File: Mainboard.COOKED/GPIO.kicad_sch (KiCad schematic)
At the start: 12 parts, among them J10 Conn_01x03_Pin, J11 Conn_01x03_Pin, J12 Conn_01x04_Pin, J13 Conn_01x04_Pin, J14 Conn_01x03_Pin, J7 Conn_01x04_Pin, J8 Conn_01x03_Pin, J9 Conn_01x04_Pin, U10 ULC0524P, U11 ULC0524P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

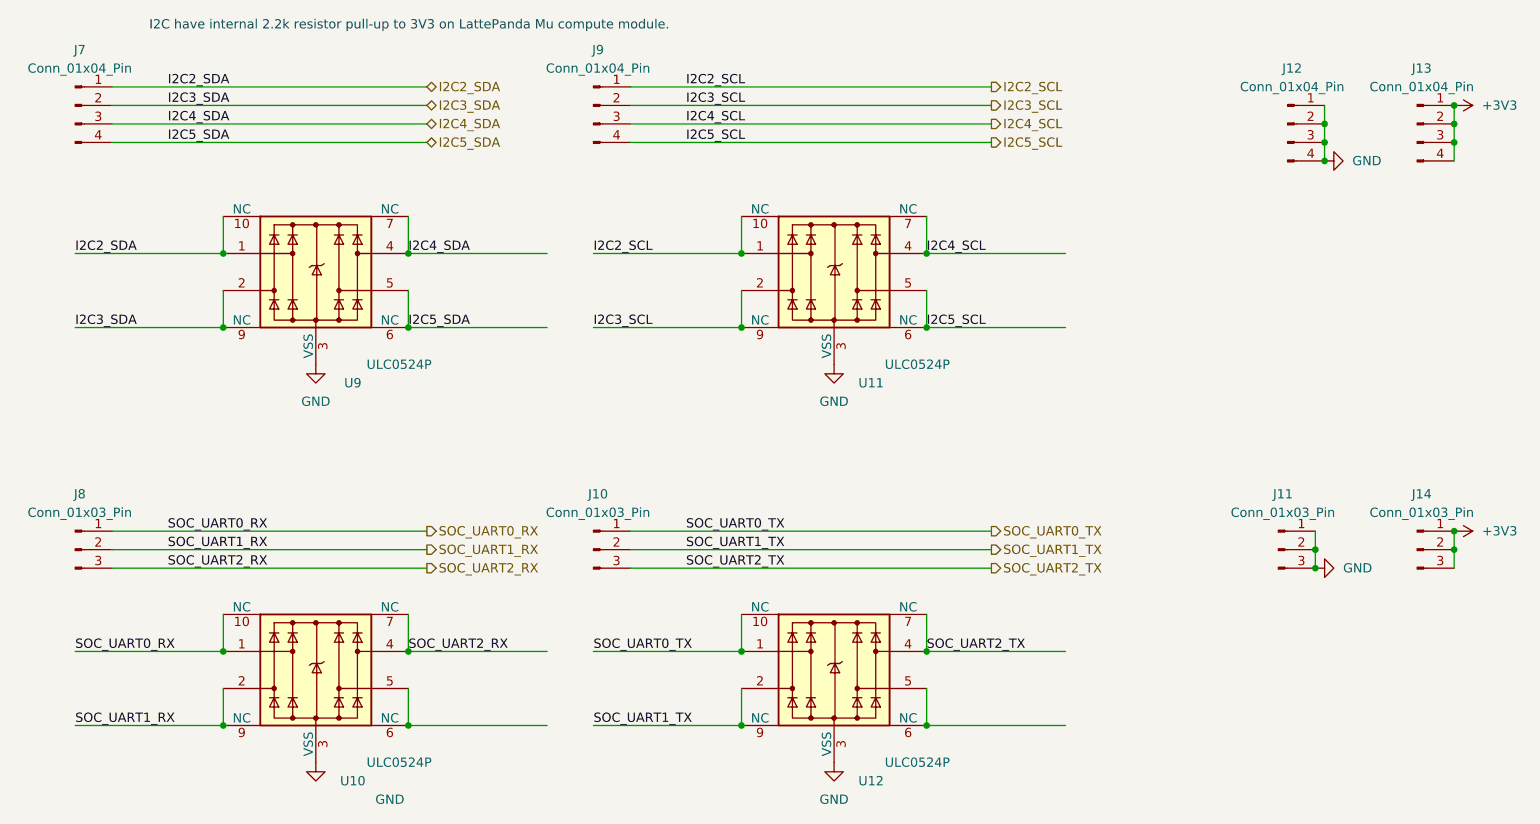
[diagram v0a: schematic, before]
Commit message: "Scrapped" the current Mainboard, seems to be very broken for no reason.
It is being kept for now so that work done for the displays can be copied over later.
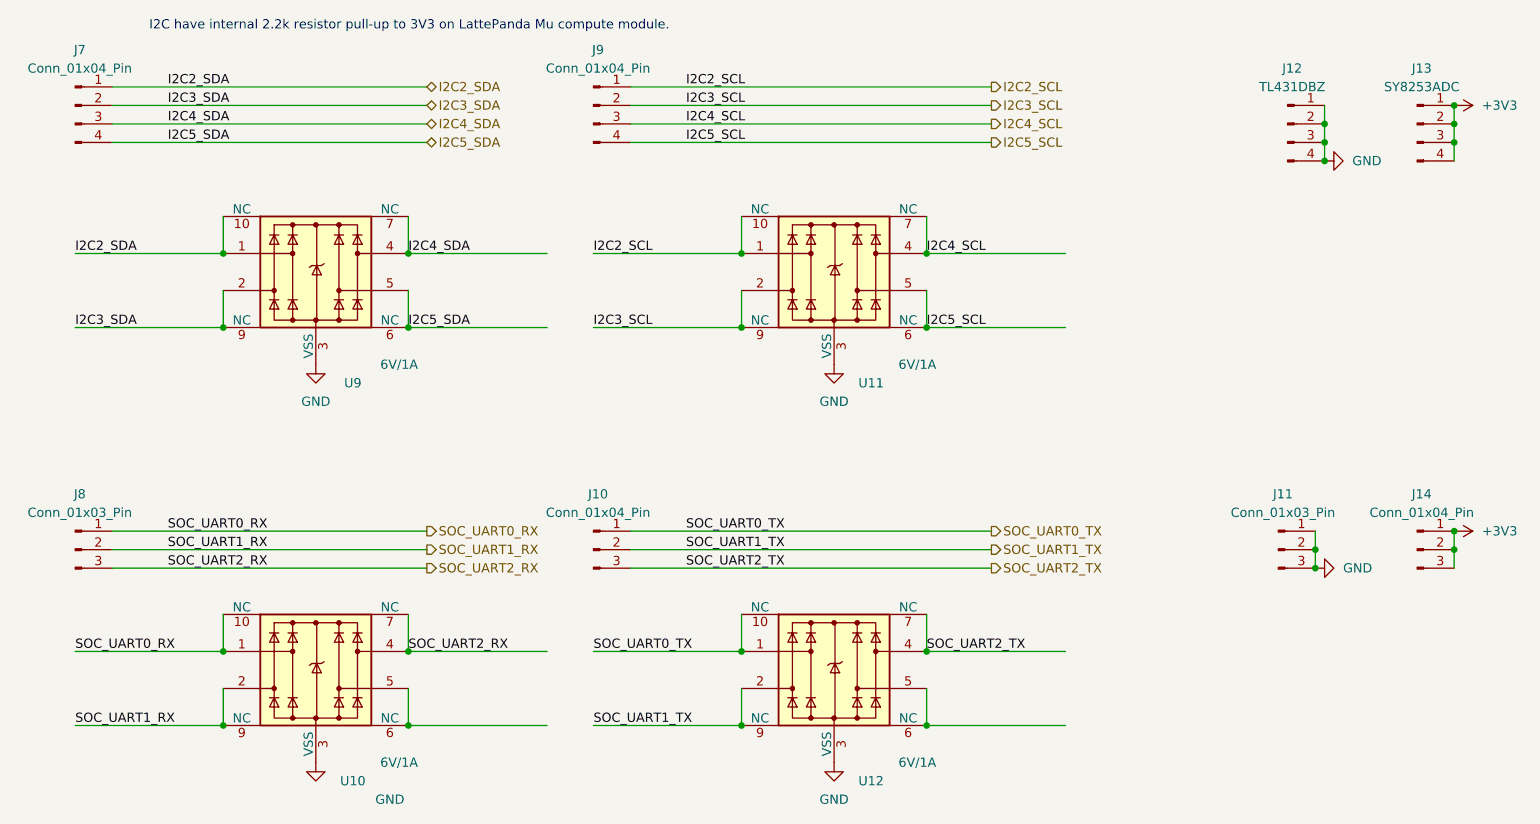
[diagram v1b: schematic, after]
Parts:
- J10: value Conn_01x03_Pin -> Conn_01x04_Pin; footprint A_HDJ_Library:PinHeader_1x03_P2.54mm_Vertical -> A_HDJ_Library:PinHeader_1x04_P2.54mm_Vertical; DF_Comment 2.54蓝色单排排针-3P -> 2.54绿色单排排针-4P
- J11: DF_Comment 2.54黑色单排排针-3P -> 2.54蓝色单排排针-3P
- J12: value Conn_01x04_Pin -> TL431DBZ; footprint A_HDJ_Library:PinHeader_1x04_P2.54mm_Vertical -> A_HDJ_Library:SOT-23; DF_Comment 2.54黑色单排排针-4P -> 参考电压-TL431ACDBZR-SOT23（丝印TAC）
- J13: value Conn_01x04_Pin -> SY8253ADC; footprint A_HDJ_Library:PinHeader_1x04_P2.54mm_Vertical -> A_HDJ_Library:TSOT-23-6; Buy_Link (none) -> https://item.szlcsc.com/94934.html; DF_Comment 2.54红色单排排针-4P -> DCDC同步降压芯片_SY8253ADC_TSOT23-6
- J14: value Conn_01x03_Pin -> Conn_01x04_Pin; footprint A_HDJ_Library:PinHeader_1x03_P2.54mm_Vertical -> A_HDJ_Library:PinHeader_1x04_P2.54mm_Vertical; DF_Comment 2.54红色单排排针-3P -> 2.54蓝色单排排针-4P
- J7: DF_Comment 2.54绿色单排排针-4P -> 2.54黑色单排排针-4P
- J8: DF_Comment 2.54绿色单排排针-3P -> 2.54红色单排排针-3P
- J9: DF_Comment 2.54蓝色单排排针-4P -> 2.54红色单排排针-4P
- U10, U11, U12, U9: value ULC0524P -> 6V/1A; footprint A_HDJ_Library:Diodes_UDFN-10_1.0x2.5mm_P0.5mm -> A_HDJ_Library:Fuse_0805_2012Metric; Buy_Link (none) -> https://item.szlcsc.com/947770.html; DF_Comment ESD静电保护IC-BV-ULC0524P-DFN2510-10L -> 0805贴片自恢复保险丝1A-6V_BSMD0805-100-6V; SCH_Show_Footprint (none) -> R0603
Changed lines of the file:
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@@
 			)
 		)
-		(property "Value" "Conn_01x03_Pin"
+		(property "Value" "Conn_01x04_Pin"
 			(at 290.195 223.52 0)
 			(show_name no)
@@
 			)
 		)
-		(property "Footprint" "A_HDJ_Library:PinHeader_1x03_P2.54mm_Vertical"
+		(property "Footprint" "A_HDJ_Library:PinHeader_1x04_P2.54mm_Vertical"
 			(at 289.56 228.6 0)
 			(hide yes)
@@
 			)
 		)
-		(property "DF_Comment" "2.54蓝色单排排针-3P"
+		(property "DF_Comment" "2.54绿色单排排针-4P"
 			(at 289.56 228.6 0)
 			(hide yes)
@@
 			)
 		)
-		(property "DF_Comment" "2.54蓝色单排排针-4P"
+		(property "DF_Comment" "2.54红色单排排针-4P"
 			(at 289.56 167.64 0)
 			(hide yes)
@@
 			)
 		)
-		(property "Value" "ULC0524P"
+		(property "Value" "6V/1A"
 			(at 262.89 203.2 0)
 			(show_name no)
@@
 			)
 		)
-		(property "Footprint" "A_HDJ_Library:Diodes_UDFN-10_1.0x2.5mm_P0.5mm"
+		(property "Footprint" "A_HDJ_Library:Fuse_0805_2012Metric"
 			(at 227.33 200.66 0)
 			(hide yes)
@@
 			)
 		)
-		(property "Datasheet" "https://www.diodes.com/assets/Datasheets/D3V3XA4B10LP.pdf"
+		(property "Datasheet" ""
 			(at 251.46 190.5 0)
 			(hide yes)
@@
 			)
 		)
-		(property "Buy_Link" ""
+		(property "Buy_Link" "https://item.szlcsc.com/947770.html"
 			(at 251.46 190.5 0)
 			(hide yes)
@@
 			)
 		)
-		(property "DF_Comment" "ESD静电保护IC-BV-ULC0524P-DFN2510-10L"
+		(property "DF_Comment" "0805贴片自恢复保险丝1A-6V_BSMD0805-100-6V"
 			(at 251.46 190.5 0)
 			(hide yes)
@@
 			)
 		)
-		(property "SCH_Show_Footprint" ""
+		(property "SCH_Show_Footprint" "R0603"
 			(at 251.46 190.5 0)
 			(hide yes)
@@
 			)
 		)
-		(property "Value" "ULC0524P"
+		(property "Value" "6V/1A"
 			(at 334.01 203.2 0)
 			(show_name no)
@@
 			)
 		)
-		(property "Footprint" "A_HDJ_Library:Diodes_UDFN-10_1.0x2.5mm_P0.5mm"
+		(property "Footprint" "A_HDJ_Library:Fuse_0805_2012Metric"
 			(at 298.45 200.66 0)
 			(hide yes)
@@
 			)
 		)
-		(property "Datasheet" "https://www.diodes.com/assets/Datasheets/D3V3XA4B10LP.pdf"
+		(property "Datasheet" ""
 			(at 322.58 190.5 0)
 			(hide yes)
@@
 			)
 		)
-		(property "Buy_Link" ""
+		(property "Buy_Link" "https://item.szlcsc.com/947770.html"
 			(at 322.58 190.5 0)
 			(hide yes)
@@
 			)
 		)
-		(property "DF_Comment" "ESD静电保护IC-BV-ULC0524P-DFN2510-10L"
+		(property "DF_Comment" "0805贴片自恢复保险丝1A-6V_BSMD0805-100-6V"
 			(at 322.58 190.5 0)
 			(hide yes)
@@
 			)
 		)
-		(property "SCH_Show_Footprint" ""
+		(property "SCH_Show_Footprint" "R0603"
 			(at 322.58 190.5 0)
 			(hide yes)
@@
 			)
 		)
-		(property "DF_Comment" "2.54绿色单排排针-4P"
+		(property "DF_Comment" "2.54黑色单排排针-4P"
 			(at 218.44 167.64 0)
 			(hide yes)
@@
 			)
 		)
-		(property "DF_Comment" "2.54绿色单排排针-3P"
+		(property "DF_Comment" "2.54红色单排排针-3P"
 			(at 218.44 228.6 0)
 			(hide yes)
@@
 			)
 		)
-		(property "DF_Comment" "2.54黑色单排排针-3P"
+		(property "DF_Comment" "2.54蓝色单排排针-3P"
 			(at 383.54 228.6 0)
 			(hide yes)
@@
 			)
 		)
-		(property "Value" "ULC0524P"
+		(property "Value" "6V/1A"
 			(at 262.89 257.81 0)
 			(show_name no)
@@
 			)
 		)
-		(property "Footprint" "A_HDJ_Library:Diodes_UDFN-10_1.0x2.5mm_P0.5mm"
+		(property "Footprint" "A_HDJ_Library:Fuse_0805_2012Metric"
 			(at 227.33 255.27 0)
 			(hide yes)
@@
 			)
 		)
-		(property "Datasheet" "https://www.diodes.com/assets/Datasheets/D3V3XA4B10LP.pdf"
+		(property "Datasheet" ""
 			(at 251.46 245.11 0)
 			(hide yes)
@@
 			)
 		)
-		(property "Buy_Link" ""
+		(property "Buy_Link" "https://item.szlcsc.com/947770.html"
 			(at 251.46 245.11 0)
 			(hide yes)
@@
 			)
 		)
-		(property "DF_Comment" "ESD静电保护IC-BV-ULC0524P-DFN2510-10L"
+		(property "DF_Comment" "0805贴片自恢复保险丝1A-6V_BSMD0805-100-6V"
 			(at 251.46 245.11 0)
 			(hide yes)
@@
 			)
 		)
-		(property "SCH_Show_Footprint" ""
+		(property "SCH_Show_Footprint" "R0603"
 			(at 251.46 245.11 0)
 			(hide yes)
@@
 			)
 		)
-		(property "Value" "Conn_01x04_Pin"
+		(property "Value" "SY8253ADC"
 			(at 403.225 165.1 0)
 			(show_name no)
@@
 			)
 		)
-		(property "Footprint" "A_HDJ_Library:PinHeader_1x04_P2.54mm_Vertical"
+		(property "Footprint" "A_HDJ_Library:TSOT-23-6"
 			(at 402.59 170.18 0)
 			(hide yes)
@@
 			)
 		)
-		(property "Datasheet" ""
+		(property "Datasheet" "https://atta.szlcsc.com/upload/public/pdf/source/20180625/C93736_E75EC6FD4320D65590D2D5BF0D8B8959.pdf"
 			(at 402.59 170.18 0)
 			(hide yes)
@@
 			)
 		)
-		(property "DF_Comment" "2.54红色单排排针-4P"
+		(property "DF_Comment" "DCDC同步降压芯片_SY8253ADC_TSOT23-6"
 			(at 402.59 170.18 0)
 			(hide yes)
@@
 		)
 		(property "Field-1" ""
+			(at 402.59 170.18 0)
+			(hide yes)
+			(show_name no)
+			(do_not_autoplace no)
+			(effects
+				(font
+					(size 1.27 1.27)
+				)
+			)
+		)
+		(property "Buy_Link" "https://item.szlcsc.com/94934.html"
 			(at 402.59 170.18 0)
 			(hide yes)
@@
 			)
 		)
-		(property "Value" "Conn_01x04_Pin"
+		(property "Value" "TL431DBZ"
 			(at 385.445 165.1 0)
 			(show_name no)
@@
 			)
 		)
-		(property "Footprint" "A_HDJ_Library:PinHeader_1x04_P2.54mm_Vertical"
+		(property "Footprint" "A_HDJ_Library:SOT-23"
 			(at 384.81 170.18 0)
 			(hide yes)
@@
 			)
 		)
-		(property "Datasheet" ""
+		(property "Datasheet" "http://www.ti.com/lit/ds/symlink/tl431.pdf"
 			(at 384.81 170.18 0)
 			(hide yes)
@@
 			)
 		)
-		(property "DF_Comment" "2.54黑色单排排针-4P"
+		(property "DF_Comment" "参考电压-TL431ACDBZR-SOT23（丝印TAC）"
 			(at 384.81 170.18 0)
 			(hide yes)
@@
 			)
 		)
-		(property "Value" "Conn_01x03_Pin"
+		(property "Value" "Conn_01x04_Pin"
 			(at 403.225 223.52 0)
 			(show_name no)
@@
 			)
 		)
-		(property "Footprint" "A_HDJ_Library:PinHeader_1x03_P2.54mm_Vertical"
+		(property "Footprint" "A_HDJ_Library:PinHeader_1x04_P2.54mm_Vertical"
 			(at 402.59 228.6 0)
 			(hide yes)
@@
 			)
 		)
-		(property "DF_Comment" "2.54红色单排排针-3P"
+		(property "DF_Comment" "2.54蓝色单排排针-4P"
 			(at 402.59 228.6 0)
 			(hide yes)
@@
 			)
 		)
-		(property "Value" "ULC0524P"
+		(property "Value" "6V/1A"
 			(at 334.01 257.81 0)
 			(show_name no)
@@
 			)
 		)
-		(property "Footprint" "A_HDJ_Library:Diodes_UDFN-10_1.0x2.5mm_P0.5mm"
+		(property "Footprint" "A_HDJ_Library:Fuse_0805_2012Metric"
 			(at 298.45 255.27 0)
 			(hide yes)
@@
 			)
 		)
-		(property "Datasheet" "https://www.diodes.com/assets/Datasheets/D3V3XA4B10LP.pdf"
+		(property "Datasheet" ""
 			(at 322.58 245.11 0)
 			(hide yes)
@@
 			)
 		)
-		(property "Buy_Link" ""
+		(property "Buy_Link" "https://item.szlcsc.com/947770.html"
 			(at 322.58 245.11 0)
 			(hide yes)
@@
 			)
 		)
-		(property "DF_Comment" "ESD静电保护IC-BV-ULC0524P-DFN2510-10L"
+		(property "DF_Comment" "0805贴片自恢复保险丝1A-6V_BSMD0805-100-6V"
 			(at 322.58 245.11 0)
 			(hide yes)
@@
 			)
 		)
-		(property "SCH_Show_Footprint" ""
+		(property "SCH_Show_Footprint" "R0603"
 			(at 322.58 245.11 0)
 			(hide yes)
